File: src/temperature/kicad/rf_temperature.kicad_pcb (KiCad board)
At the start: 2 copper layers, 62.7 x 78.5 mm, 13 parts, among them J1 Conn_01x20, J2 Screw_Terminal_01x02, J3 Conn_01x20, U1 Pico, U2 DS18B20, U3 NRF24L01_Breakout

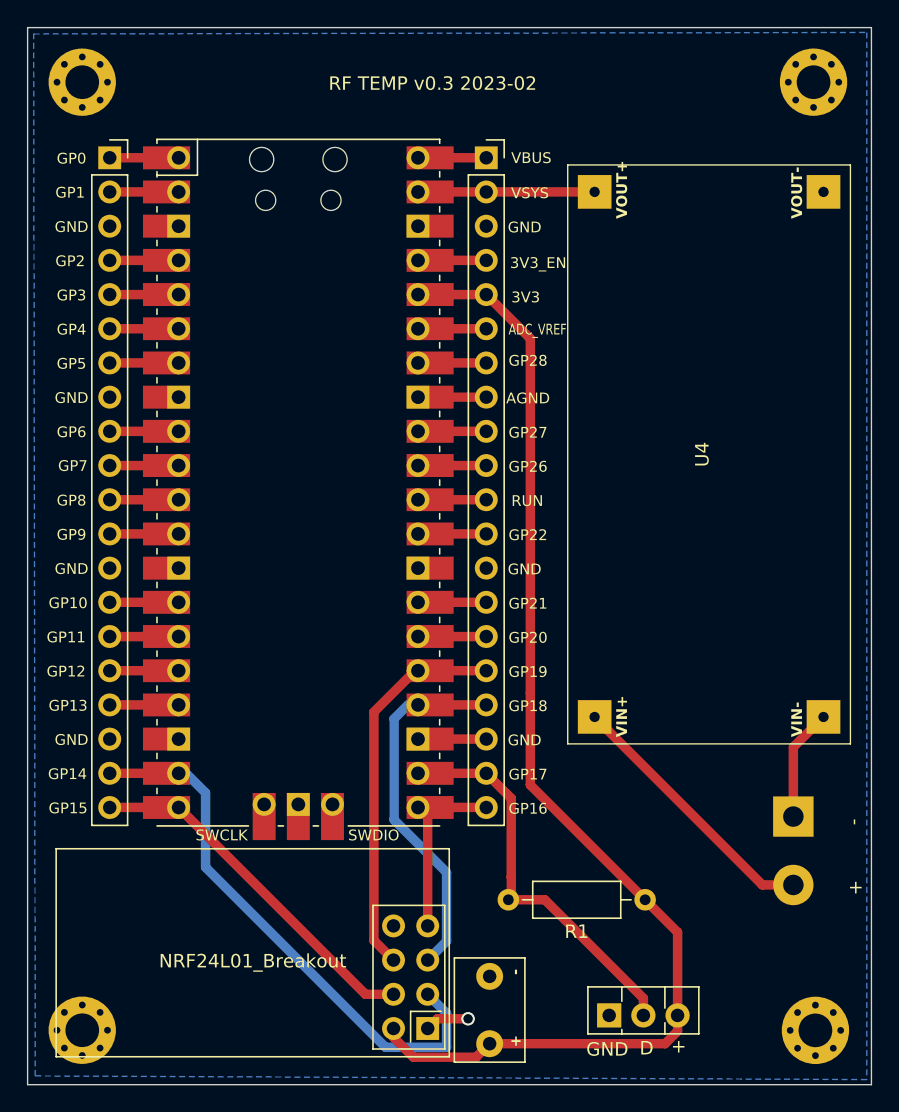
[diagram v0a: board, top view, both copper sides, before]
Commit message: use ground plane
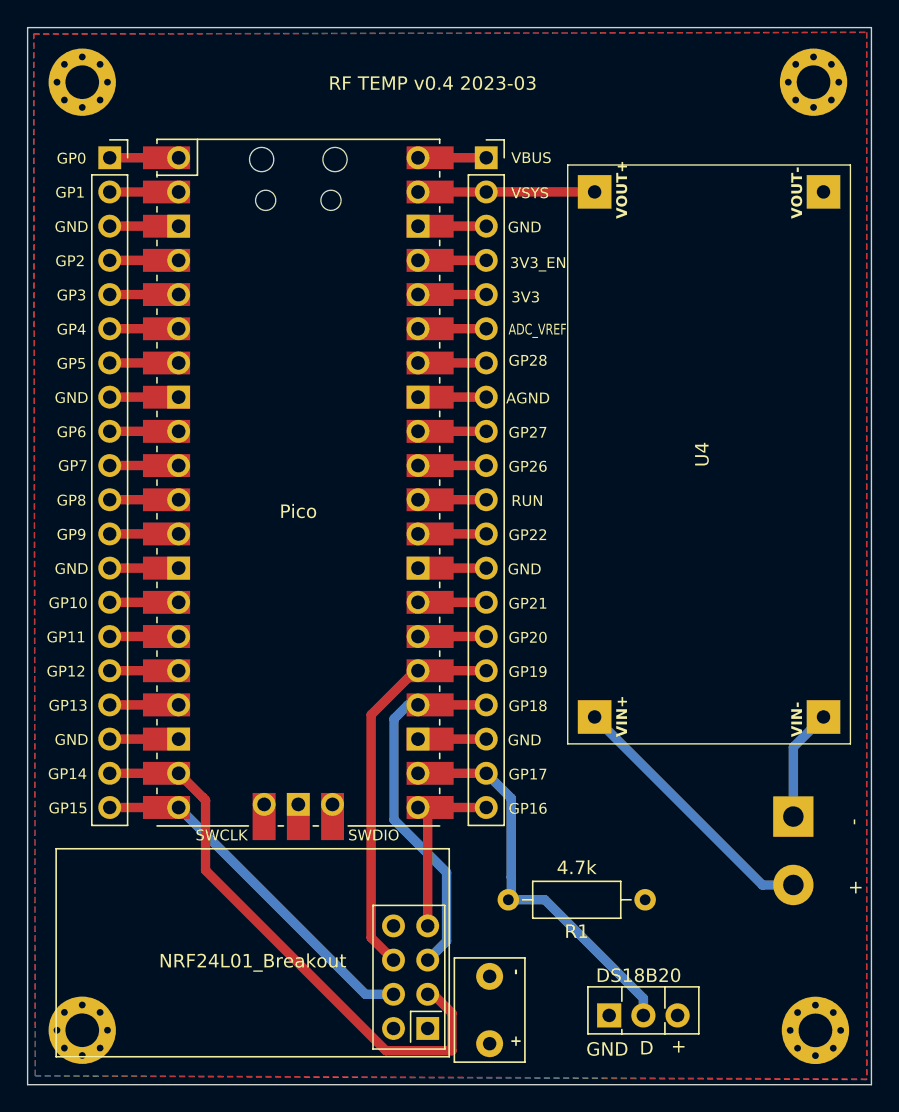
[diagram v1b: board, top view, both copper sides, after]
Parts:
- U4: footprint MyLibrary:LM2596AdjBuck -> my_LM2596_Library:my_LM2596AdjBuck
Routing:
- net 3V3: track 88.8 -> 5.07 mm
- net GND: track 8.37 -> 35.7 mm, vias 1 -> 0
- net Net-(J1-Pin_19): track 41.2 -> 42.2 mm
- added copper zone on F.Cu, net 3V3
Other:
- board text added: "RF TEMP v0.4 2023-03"
- board text removed: "RF TEMP v0.3 2023-02"
